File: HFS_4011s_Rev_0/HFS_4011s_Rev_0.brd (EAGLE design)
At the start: 47 x 44.5 mm, 44 parts, among them IC1 CP2104, J1 2X06, J2 2X12, J3 1X02, Q1 mmbt2222, Q2 mmbt2222, Q3 MMUN2133LT1G, SW2 KMR2, U1 TPS61090RSAR, U2 MCP73831T-2ACI/OT, U3 LM3940, X2 ESP32_WROOM32_SKINNY, X4 20329

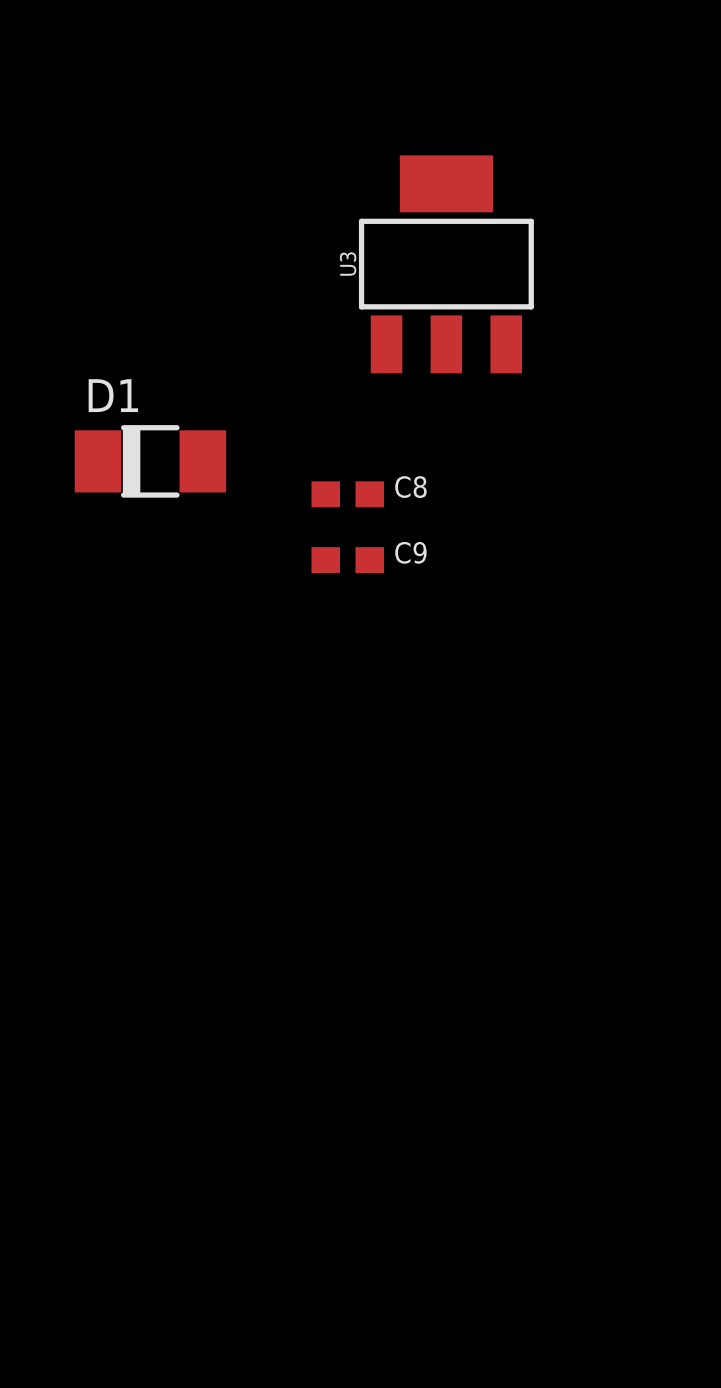
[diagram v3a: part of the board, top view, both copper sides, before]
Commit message: Added in 3.3V buck converter and got rid of 3.3V LDO.
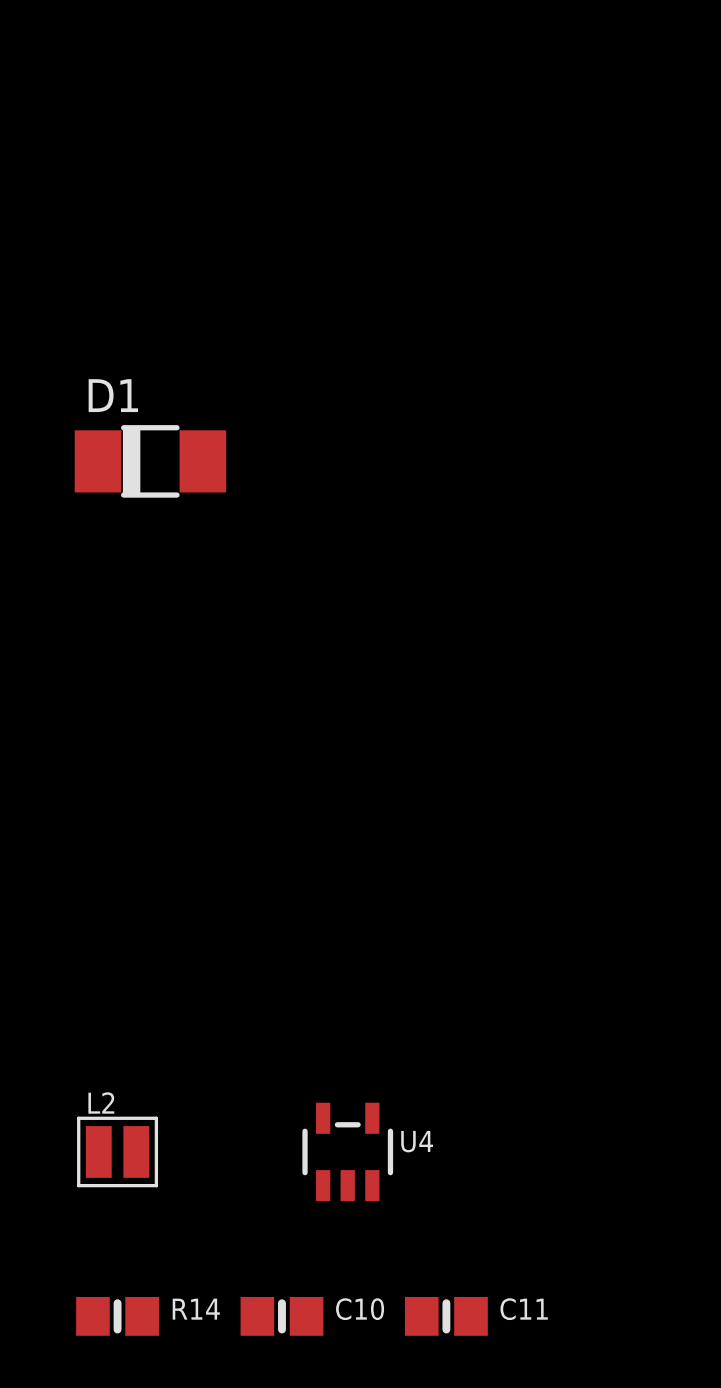
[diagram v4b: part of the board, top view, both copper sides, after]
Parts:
- removed C8: 0.47uF, microbuilder:0603-NO
- removed C9: 33uF, microbuilder:0603-NO
- removed U3: LM3940, HFS4011sCustom:SOT223
- added C10: 22uF, microbuilder:0805-NO
- added C11: 10uF, microbuilder:0805-NO
- added L2: 2.2uH/NRH2412T2R2MNGH, microbuilder:INDUCTOR_TAIYOYUDEN_NRH2412T
- added R14: 100K, microbuilder:0805-NO
- added U4: LM3671MF-3.3/NOPB, microbuilder:SOT23-5
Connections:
- new net EN: R14.2, U4.3
- new net N$17: L2.1, U4.5
- net 3.3V: now also C10.1, L2.2, U4.4; no longer C9.1, U3.3
- net 5.0V: no longer C8.1, U3.1
- net GND: now also C10.2, C11.2, U4.2; no longer C8.2, C9.2, U3.2, U3.4
- net VBAT: now also C11.1, R14.1, U4.1
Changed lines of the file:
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@@
 <element name="Q3" library="transistor" package="SC59-BEC" value="MMUN2133LT1G" x="33.02" y="-83.82"/>
 <element name="J3" library="HFS4011sCustom" package="1X02" value="1X02" x="8.89" y="-114.3"/>
-<element name="U3" library="HFS4011sCustom" package="SOT223" value="LM3940" x="6.35" y="-127"/>
-<element name="C8" library="microbuilder" package="0603-NO" value="0.47uF" x="2.54" y="-135.89"/>
-<element name="C9" library="microbuilder" package="0603-NO" value="33uF" x="2.54" y="-138.43"/>
 <element name="D1" library="HFS4011sCustom" package="DO-214AC" value="SMAJ5.0CALFDKR-ND" x="-5.08" y="-134.62"/>
+<element name="U4" library="microbuilder" package="SOT23-5" value="LM3671MF-3.3/NOPB" x="2.54" y="-161.29"/>
+<element name="L2" library="microbuilder" package="INDUCTOR_TAIYOYUDEN_NRH2412T" value="2.2uH/NRH2412T2R2MNGH" x="-6.35" y="-161.29"/>
+<element name="C10" library="microbuilder" package="0805-NO" value="22uF" x="0" y="-167.64"/>
+<element name="C11" library="microbuilder" package="0805-NO" value="10uF" x="6.35" y="-167.64"/>
+<element name="R14" library="microbuilder" package="0805-NO" value="100K" x="-6.35" y="-167.64"/>
 </elements>
 <signals>
@@
 <contactref element="R11" pad="1"/>
 <contactref element="LBO" pad="C"/>
-<contactref element="C8" pad="2"/>
-<contactref element="U3" pad="4"/>
-<contactref element="U3" pad="2"/>
-<contactref element="C9" pad="2"/>
 <contactref element="D1" pad="A"/>
 <polygon width="0.1524" layer="1">
@@
 <vertex x="-8.89" y="-5.08"/>
 </polygon>
-<wire x1="3.39" y1="-135.89" x2="-3.055" y2="-134.62" width="0" layer="19" extent="1-1"/>
-<wire x1="3.39" y1="-138.43" x2="3.39" y2="-135.89" width="0" layer="19" extent="1-1"/>
-<wire x1="6.35" y1="-130.0988" x2="3.39" y2="-135.89" width="0" layer="19" extent="1-1"/>
-<wire x1="6.35" y1="-123.901" x2="6.35" y2="-130.0988" width="0" layer="19" extent="1-1"/>
-<wire x1="9.84" y1="-104.14" x2="6.35" y2="-123.901" width="0" layer="19" extent="1-1"/>
+<contactref element="U4" pad="2"/>
+<contactref element="C10" pad="2"/>
+<contactref element="C11" pad="2"/>
+<wire x1="2.54" y1="-162.5901" x2="0.95" y2="-167.64" width="0" layer="19" extent="1-1"/>
+<wire x1="7.3" y1="-167.64" x2="0.95" y2="-167.64" width="0" layer="19" extent="1-1"/>
+<wire x1="-3.055" y1="-134.62" x2="2.54" y2="-162.5901" width="0" layer="19" extent="1-1"/>
+<wire x1="1.59" y1="-104.14" x2="-3.055" y2="-134.62" width="0" layer="19" extent="1-1"/>
+<wire x1="9.84" y1="-104.14" x2="1.59" y2="-104.14" width="0" layer="19" extent="1-1"/>
 <wire x1="16.19" y1="-104.14" x2="9.84" y2="-104.14" width="0" layer="19" extent="1-1"/>
 <wire x1="16.83" y1="-99.06" x2="16.19" y2="-104.14" width="0" layer="19" extent="1-1"/>
 <wire x1="22.54" y1="-104.14" x2="16.19" y2="-104.14" width="0" layer="19" extent="1-1"/>
 <wire x1="27.94" y1="-103.09" x2="22.54" y2="-104.14" width="0" layer="19" extent="1-1"/>
-<wire x1="1.59" y1="-104.14" x2="9.84" y2="-104.14" width="0" layer="19" extent="1-1"/>
 <wire x1="37.78" y1="-99.06" x2="27.94" y2="-103.09" width="0" layer="19" extent="1-1"/>
 <wire x1="15.565" y1="-88.46" x2="16.83" y2="-99.06" width="0" layer="19" extent="1-1"/>
@@
 <wire x1="20.32" y1="-34.51" x2="9.84" y2="-36.83" width="0" layer="19" extent="1-1"/>
 <wire x1="22.11" y1="3.08" x2="20.32" y2="-34.51" width="0" layer="19" extent="1-1"/>
-<wire x1="7.62" y1="30.48" x2="5.62" y2="31.23" width="0" layer="19" extent="1-1"/>
+<wire x1="23.61" y1="3.08" x2="22.11" y2="3.08" width="0" layer="19" extent="1-1"/>
+<wire x1="24.16" y1="5.855" x2="23.61" y2="3.08" width="0" layer="19" extent="1-1"/>
+<wire x1="26.16" y1="5.98" x2="24.16" y2="5.855" width="0" layer="19" extent="1-1"/>
 <wire x1="26.46" y1="3.18" x2="26.16" y2="5.98" width="0" layer="19" extent="1-1"/>
-<wire x1="19.26" y1="3.18" x2="19.56" y2="5.98" width="0" layer="19" extent="1-1"/>
+<wire x1="19.26" y1="3.18" x2="22.11" y2="3.08" width="0" layer="19" extent="1-1"/>
+<wire x1="19.56" y1="5.98" x2="19.26" y2="3.18" width="0" layer="19" extent="1-1"/>
+<wire x1="17.16" y1="11.23" x2="19.56" y2="5.98" width="0" layer="19" extent="1-1"/>
+<wire x1="23.2" y1="21.43" x2="17.16" y2="11.23" width="0" layer="19" extent="1-1"/>
+<wire x1="31.36" y1="29.13" x2="23.2" y2="21.43" width="0" layer="19" extent="1-1"/>
+<wire x1="14.36" y1="29.13" x2="23.2" y2="21.43" width="0" layer="19" extent="1-1"/>
+<wire x1="11.11" y1="25.4" x2="14.36" y2="29.13" width="0" layer="19" extent="1-1"/>
+<wire x1="8.4" y1="21.12" x2="11.11" y2="25.4" width="0" layer="19" extent="1-1"/>
+<wire x1="4.3" y1="21.12" x2="8.4" y2="21.12" width="0" layer="19" extent="1-1"/>
+<wire x1="7.62" y1="30.48" x2="11.11" y2="25.4" width="0" layer="19" extent="1-1"/>
+<wire x1="5.62" y1="31.23" x2="7.62" y2="30.48" width="0" layer="19" extent="1-1"/>
+<wire x1="1.69" y1="38.1" x2="5.62" y2="31.23" width="0" layer="19" extent="1-1"/>
+<wire x1="3.39" y1="41.91" x2="1.69" y2="38.1" width="0" layer="19" extent="1-1"/>
+<wire x1="7.62" y1="41.69" x2="3.39" y2="41.91" width="0" layer="19" extent="1-1"/>
 </signal>
 <signal name="VBUS">
@@
 <contactref element="J3" pad="2"/>
 <contactref element="D1" pad="C"/>
+<contactref element="R14" pad="1"/>
+<contactref element="U4" pad="1"/>
+<contactref element="C11" pad="1"/>
+<wire x1="1.59" y1="-162.5901" x2="-7.3" y2="-167.64" width="0" layer="19" extent="1-1"/>
+<wire x1="5.4" y1="-167.64" x2="1.59" y2="-162.5901" width="0" layer="19" extent="1-1"/>
+<wire x1="-7.105" y1="-134.62" x2="1.59" y2="-162.5901" width="0" layer="19" extent="1-1"/>
 <wire x1="10.16" y1="-114.3" x2="-7.105" y2="-134.62" width="0" layer="19" extent="1-1"/>
 <wire x1="7.94" y1="-104.14" x2="10.16" y2="-114.3" width="0" layer="19" extent="1-1"/>
@@
 <contactref element="X2" pad="2"/>
 <contactref element="R13" pad="3"/>
-<contactref element="C9" pad="1"/>
-<contactref element="U3" pad="3"/>
-<wire x1="8.6614" y1="-130.0988" x2="1.69" y2="-138.43" width="0" layer="19" extent="1-1"/>
-<wire x1="8.02" y1="6.77" x2="8.6614" y2="-130.0988" width="0" layer="19" extent="1-1"/>
+<contactref element="U4" pad="4"/>
+<contactref element="L2" pad="2"/>
+<contactref element="C10" pad="1"/>
+<wire x1="-5.625" y1="-161.29" x2="-0.95" y2="-167.64" width="0" layer="19" extent="1-1"/>
+<wire x1="3.49" y1="-159.9899" x2="-0.95" y2="-167.64" width="0" layer="19" extent="1-1"/>
+<wire x1="8.02" y1="6.77" x2="3.49" y2="-159.9899" width="0" layer="19" extent="1-1"/>
 <wire x1="9.21" y1="25.4" x2="8.02" y2="6.77" width="0" layer="19" extent="1-1"/>
 <wire x1="6.37" y1="28.48" x2="9.21" y2="25.4" width="0" layer="19" extent="1-1"/>
@@
 <contactref element="R4" pad="2"/>
 <contactref element="C7" pad="+"/>
-<contactref element="C8" pad="1"/>
-<contactref element="U3" pad="1"/>
-<wire x1="4.0386" y1="-130.0988" x2="1.69" y2="-135.89" width="0" layer="19" extent="1-1"/>
-<wire x1="14.29" y1="-104.14" x2="4.0386" y2="-130.0988" width="0" layer="19" extent="1-1"/>
-<wire x1="3.49" y1="-99.06" x2="14.29" y2="-104.14" width="0" layer="19" extent="1-1"/>
+<wire x1="14.29" y1="-104.14" x2="3.49" y2="-99.06" width="0" layer="19" extent="1-1"/>
 <wire x1="13.14" y1="-85.385" x2="3.49" y2="-99.06" width="0" layer="19" extent="1-1"/>
 <wire x1="14.265" y1="-84.26" x2="13.14" y2="-85.385" width="0" layer="19" extent="1-1"/>
@@
 <wire x1="6.08" y1="-91.33" x2="7.62" y2="-114.3" width="0" layer="19" extent="1-1"/>
 </signal>
+<signal name="N$17">
+<contactref element="L2" pad="1"/>
+<contactref element="U4" pad="5"/>
+<wire x1="1.59" y1="-159.9899" x2="-7.075" y2="-161.29" width="0" layer="19" extent="1-1"/>
+</signal>
+<signal name="EN">
+<contactref element="U4" pad="3"/>
+<contactref element="R14" pad="2"/>
+<wire x1="3.49" y1="-162.5901" x2="-5.4" y2="-167.64" width="0" layer="19" extent="1-1"/>
+</signal>
 </signals>

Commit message: Added in DAC
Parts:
- removed X4: 20329, microbuilder:4UCONN_20329_V2
- added C12: 10nF, rcl:C0603
- added C13, C14: 10uF, SparkFun-Retired:EIA3216
- added C8, C9: 0.1uF, rcl:C0603
- added J4: (no value), SparkFun-Connectors:USB-C-16P
- added R15, R16: 5.1k, rcl:R0603
- added R17: 5k, rcl:R0603
- added R18: (no value), rcl:R0603
- added U3: AD5693R, HFS4011sCustom:MSOP10
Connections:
- new net DAC_OUT: U3.10
- new net N$18: J4.A5, R16.2
- new net N$19: J4.B5, R15.2
- new net N$20: C12.1, U3.9
- net 3.3V: now also C13.A, C14.A, C8.1, C9.1, R17.2, R18.2, U3.1, U3.2, U3.3
- net GND: now also C12.2, C13.C, C14.C, C8.2, C9.2, J4.GND, J4.GND2, R15.1, R16.1, U3.4, U3.5, U3.6; no longer X4.BASE@1, X4.BASE@2, X4.GND, X4.SPRT@1, X4.SPRT@2, X4.SPRT@3, X4.SPRT@4
- net N$2: now also J4.A6, J4.B6; no longer X4.D+
- net N$6: now also J4.A7, J4.B7; no longer X4.D-
- net SCL: now also R17.1, U3.7
- net SDA: now also R18.1, U3.8
- net VBUS: now also J4.VBUS1, J4.VBUS2; no longer X4.VBUS

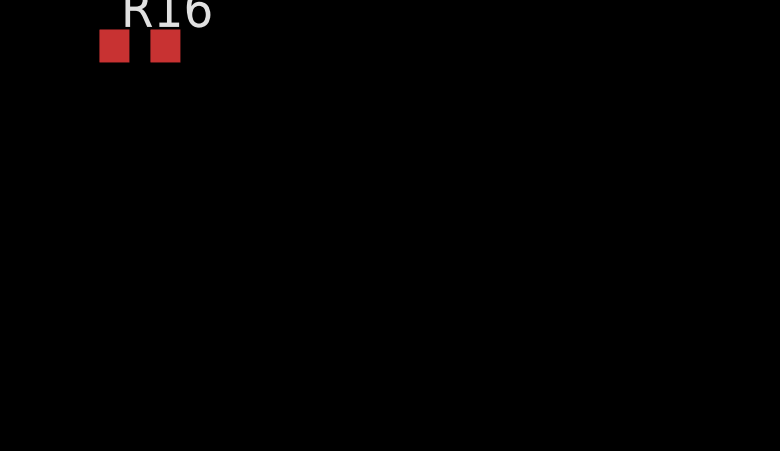
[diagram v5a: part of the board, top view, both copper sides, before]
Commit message: Added labels for FPAA IO. Still determining peripherals.
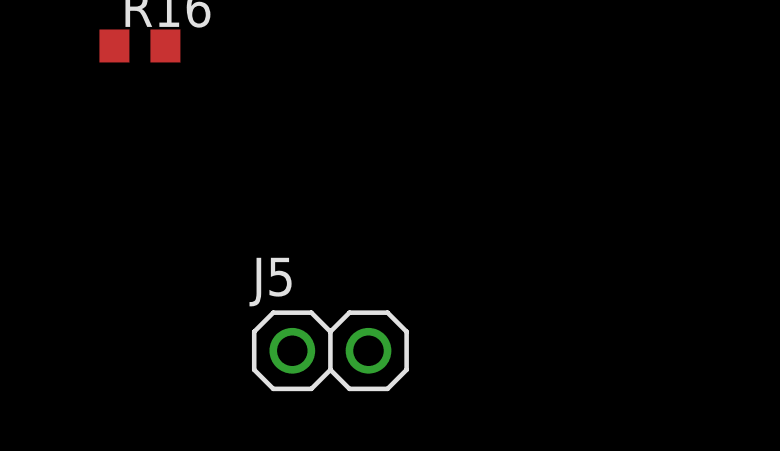
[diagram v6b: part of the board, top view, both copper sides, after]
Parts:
- added J5: 1X02, HFS4011sCustom:1X02
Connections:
- new net E0: J2.23
- new net E1: J2.21
- new net E2: J2.19
- new net E3: J2.12
- new net E4: J2.10
- new net N$27: J2.14
- new net N$28: J2.16
- new net N$29: J2.18
- new net N$39: J2.13
- new net N$40: J2.15
- new net N$41: J2.17
- new net S0: J2.8
- new net S1: J1.8, J2.6
- new net S2: J2.4
- new net S3: J1.10, J2.2
- new net S4: J2.11
- new net S5: J1.12, J2.9
- new net S6: J2.7
- new net S7: J2.5
- new net S8: J2.3
- new net S9: J2.1
- new net W1: J2.24
- new net W3: J2.22
- new net W4: J2.20
- net 5.0V: now also J5.1
- net GND: now also J5.2
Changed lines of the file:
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@@
 <element name="R15" library="rcl" library_urn="urn:adsk.eagle:library:334" package="R0603" package3d_urn="urn:adsk.eagle:package:23555/2" value="5.1k" x="-15.24" y="-229.87"/>
 <element name="R16" library="rcl" library_urn="urn:adsk.eagle:library:334" package="R0603" package3d_urn="urn:adsk.eagle:package:23555/2" value="5.1k" x="-15.24" y="-234.95"/>
+<element name="J5" library="HFS4011sCustom" package="1X02" value="1X02" x="-8.89" y="-245.11"/>
 </elements>
 <signals>
@@
 <contactref element="R15" pad="1"/>
 <contactref element="R16" pad="1"/>
+<contactref element="J5" pad="2"/>
+<wire x1="-16.09" y1="-234.95" x2="-7.62" y2="-245.11" width="0" layer="19" extent="1-1"/>
 <wire x1="-16.09" y1="-229.87" x2="-16.09" y2="-234.95" width="0" layer="19" extent="1-1"/>
 <wire x1="-15.37" y1="-213.36" x2="-16.09" y2="-229.87" width="0" layer="19" extent="1-1"/>
@@
 <contactref element="R4" pad="2"/>
 <contactref element="C7" pad="+"/>
+<contactref element="J5" pad="1"/>
 <wire x1="14.29" y1="-104.14" x2="3.49" y2="-99.06" width="0" layer="19" extent="1-1"/>
 <wire x1="13.14" y1="-85.385" x2="3.49" y2="-99.06" width="0" layer="19" extent="1-1"/>
@@
 <wire x1="25.655" y1="-85.09" x2="14.915" y2="-84.26" width="0" layer="19" extent="1-1"/>
 <wire x1="33.02" y1="-105.19" x2="14.29" y2="-104.14" width="0" layer="19" extent="1-1"/>
+<wire x1="-10.16" y1="-245.11" x2="14.29" y2="-104.14" width="0" layer="19" extent="1-1"/>
 </signal>
 <signal name="N$10">
@@
 <wire x1="-14.47" y1="-187.1169" x2="-14.82" y2="-203.2" width="0" layer="19" extent="1-1"/>
 </signal>
+<signal name="S5">
+<contactref element="J1" pad="12"/>
+<contactref element="J2" pad="9"/>
+<wire x1="41.91" y1="15.24" x2="26.67" y2="39.37" width="0" layer="19" extent="1-1"/>
+</signal>
+<signal name="S3">
+<contactref element="J1" pad="10"/>
+<contactref element="J2" pad="2"/>
+<wire x1="41.91" y1="12.7" x2="16.51" y2="41.91" width="0" layer="19" extent="1-1"/>
+</signal>
+<signal name="S1">
+<contactref element="J1" pad="8"/>
+<contactref element="J2" pad="6"/>
+<wire x1="41.91" y1="10.16" x2="21.59" y2="41.91" width="0" layer="19" extent="1-1"/>
+</signal>
+<signal name="S2">
+<contactref element="J2" pad="4"/>
+</signal>
+<signal name="S0">
+<contactref element="J2" pad="8"/>
+</signal>
+<signal name="E4">
+<contactref element="J2" pad="10"/>
+</signal>
+<signal name="E3">
+<contactref element="J2" pad="12"/>
+</signal>
+<signal name="N$27">
+<contactref element="J2" pad="14"/>
+</signal>
+<signal name="N$28">
+<contactref element="J2" pad="16"/>
+</signal>
+<signal name="N$29">
+<contactref element="J2" pad="18"/>
+</signal>
+<signal name="W4">
+<contactref element="J2" pad="20"/>
+</signal>
+<signal name="W3">
+<contactref element="J2" pad="22"/>
+</signal>
+<signal name="W1">
+<contactref element="J2" pad="24"/>
+</signal>
+<signal name="S9">
+<contactref element="J2" pad="1"/>
+</signal>
+<signal name="S8">
+<contactref element="J2" pad="3"/>
+</signal>
+<signal name="S7">
+<contactref element="J2" pad="5"/>
+</signal>
+<signal name="S6">
+<contactref element="J2" pad="7"/>
+</signal>
+<signal name="S4">
+<contactref element="J2" pad="11"/>
+</signal>
+<signal name="N$39">
+<contactref element="J2" pad="13"/>
+</signal>
+<signal name="N$40">
+<contactref element="J2" pad="15"/>
+</signal>
+<signal name="N$41">
+<contactref element="J2" pad="17"/>
+</signal>
+<signal name="E2">
+<contactref element="J2" pad="19"/>
+</signal>
+<signal name="E1">
+<contactref element="J2" pad="21"/>
+</signal>
+<signal name="E0">
+<contactref element="J2" pad="23"/>
+</signal>
 </signals>
